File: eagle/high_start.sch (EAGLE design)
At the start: 37 parts, among them IC1 7805L, Q1 16Mhz, Q2 IRF510, Q3 IRF510, Q4 IRF510, U2 ATMEGA328P_PDIP

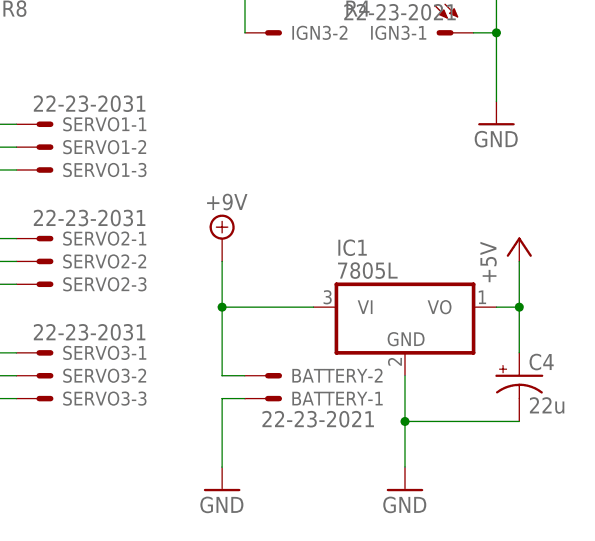
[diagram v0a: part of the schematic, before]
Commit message: pulldowns placed
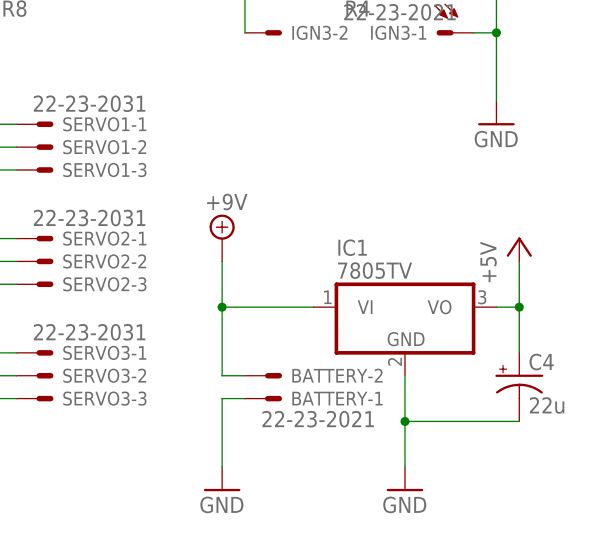
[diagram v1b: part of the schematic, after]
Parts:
- IC1: value 7805L -> 7805TV; device linear:7805L -> linear:7805TV
- R10, R6, R9: device rcl:R-US_0207/7 -> rcl:R-US_0207/2V
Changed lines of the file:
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@@
 <grid distance="0.1" unitdist="inch" unit="inch" style="lines" multiple="1" display="no" altdistance="0.01" altunitdist="inch" altunit="inch"/>
 <layers>
-<layer number="1" name="Top" color="4" fill="1" visible="no" active="no"/>
-<layer number="16" name="Bottom" color="1" fill="1" visible="no" active="no"/>
-<layer number="17" name="Pads" color="2" fill="1" visible="no" active="no"/>
-<layer number="18" name="Vias" color="2" fill="1" visible="no" active="no"/>
-<layer number="19" name="Unrouted" color="6" fill="1" visible="no" active="no"/>
-<layer number="20" name="Dimension" color="15" fill="1" visible="no" active="no"/>
-<layer number="21" name="tPlace" color="7" fill="1" visible="no" active="no"/>
-<layer number="22" name="bPlace" color="7" fill="1" visible="no" active="no"/>
-<layer number="23" name="tOrigins" color="15" fill="1" visible="no" active="no"/>
-<layer number="24" name="bOrigins" color="15" fill="1" visible="no" active="no"/>
-<layer number="25" name="tNames" color="7" fill="1" visible="no" active="no"/>
-<layer number="26" name="bNames" color="7" fill="1" visible="no" active="no"/>
-<layer number="27" name="tValues" color="7" fill="1" visible="no" active="no"/>
-<layer number="28" name="bValues" color="7" fill="1" visible="no" active="no"/>
+<layer number="1" name="Top" color="4" fill="1" visible="yes" active="no"/>
+<layer number="16" name="Bottom" color="1" fill="1" visible="yes" active="no"/>
+<layer number="17" name="Pads" color="2" fill="1" visible="yes" active="no"/>
+<layer number="18" name="Vias" color="2" fill="1" visible="yes" active="no"/>
+<layer number="19" name="Unrouted" color="6" fill="1" visible="yes" active="no"/>
+<layer number="20" name="Dimension" color="15" fill="1" visible="yes" active="no"/>
+<layer number="21" name="tPlace" color="7" fill="1" visible="yes" active="no"/>
+<layer number="22" name="bPlace" color="7" fill="1" visible="yes" active="no"/>
+<layer number="23" name="tOrigins" color="15" fill="1" visible="yes" active="no"/>
+<layer number="24" name="bOrigins" color="15" fill="1" visible="yes" active="no"/>
+<layer number="25" name="tNames" color="7" fill="1" visible="yes" active="no"/>
+<layer number="26" name="bNames" color="7" fill="1" visible="yes" active="no"/>
+<layer number="27" name="tValues" color="7" fill="1" visible="yes" active="no"/>
+<layer number="28" name="bValues" color="7" fill="1" visible="yes" active="no"/>
 <layer number="29" name="tStop" color="7" fill="3" visible="no" active="no"/>
 <layer number="30" name="bStop" color="7" fill="6" visible="no" active="no"/>
@@
 <layer number="35" name="tGlue" color="7" fill="4" visible="no" active="no"/>
 <layer number="36" name="bGlue" color="7" fill="5" visible="no" active="no"/>
-<layer number="37" name="tTest" color="7" fill="1" visible="no" active="no"/>
-<layer number="38" name="bTest" color="7" fill="1" visible="no" active="no"/>
+<layer number="37" name="tTest" color="7" fill="1" visible="yes" active="no"/>
+<layer number="38" name="bTest" color="7" fill="1" visible="yes" active="no"/>
 <layer number="39" name="tKeepout" color="4" fill="11" visible="no" active="no"/>
 <layer number="40" name="bKeepout" color="1" fill="11" visible="no" active="no"/>
@@
 <layer number="44" name="Drills" color="7" fill="1" visible="no" active="no"/>
 <layer number="45" name="Holes" color="7" fill="1" visible="no" active="no"/>
-<layer number="46" name="Milling" color="3" fill="1" visible="no" active="no"/>
-<layer number="47" name="Measures" color="7" fill="1" visible="no" active="no"/>
-<layer number="48" name="Document" color="7" fill="1" visible="no" active="no"/>
-<layer number="49" name="Reference" color="7" fill="1" visible="no" active="no"/>
-<layer number="50" name="dxf" color="7" fill="1" visible="no" active="no"/>
-<layer number="51" name="tDocu" color="7" fill="1" visible="no" active="no"/>
-<layer number="52" name="bDocu" color="7" fill="1" visible="no" active="no"/>
-<layer number="53" name="tGND_GNDA" color="7" fill="9" visible="no" active="no"/>
-<layer number="54" name="bGND_GNDA" color="1" fill="9" visible="no" active="no"/>
-<layer number="56" name="wert" color="7" fill="1" visible="no" active="no"/>
-<layer number="57" name="tCAD" color="7" fill="1" visible="no" active="no"/>
-<layer number="59" name="tCarbon" color="7" fill="1" visible="no" active="no"/>
-<layer number="60" name="bCarbon" color="7" fill="1" visible="no" active="no"/>
+<layer number="46" name="Milling" color="3" fill="1" visible="yes" active="no"/>
+<layer number="47" name="Measures" color="7" fill="1" visible="yes" active="no"/>
+<layer number="48" name="Document" color="7" fill="1" visible="yes" active="no"/>
+<layer number="49" name="Reference" color="7" fill="1" visible="yes" active="no"/>
+<layer number="50" name="dxf" color="7" fill="1" visible="yes" active="no"/>
+<layer number="51" name="tDocu" color="7" fill="1" visible="yes" active="no"/>
+<layer number="52" name="bDocu" color="7" fill="1" visible="yes" active="no"/>
+<layer number="53" name="tGND_GNDA" color="7" fill="9" visible="yes" active="no"/>
+<layer number="54" name="bGND_GNDA" color="1" fill="9" visible="yes" active="no"/>
+<layer number="56" name="wert" color="7" fill="1" visible="yes" active="no"/>
+<layer number="57" name="tCAD" color="7" fill="1" visible="yes" active="no"/>
+<layer number="59" name="tCarbon" color="7" fill="1" visible="yes" active="no"/>
+<layer number="60" name="bCarbon" color="7" fill="1" visible="yes" active="no"/>
 <layer number="90" name="Modules" color="5" fill="1" visible="yes" active="yes"/>
 <layer number="91" name="Nets" color="2" fill="1" visible="yes" active="yes"/>
@@
 <part name="P+5" library="supply1" deviceset="+5V" device=""/>
 <part name="GND7" library="supply1" deviceset="GND" device=""/>
-<part name="IC1" library="linear" deviceset="78*" device="L" technology="05"/>
+<part name="IC1" library="linear" deviceset="78*" device="TV" technology="05" value="7805TV"/>
 <part name="SUPPLY2" library="supply2" deviceset="+9V" device=""/>
 <part name="C4" library="rcl" deviceset="CPOL-US" device="B45181A" value="22u"/>
@@
 <part name="GND9" library="supply1" deviceset="GND" device=""/>
 <part name="R5" library="rcl" deviceset="R-US_" device="0207/7" value="220"/>
-<part name="R6" library="rcl" deviceset="R-US_" device="0207/7" value="10k"/>
+<part name="R6" library="rcl" deviceset="R-US_" device="0207/2V" value="10k"/>
 <part name="R7" library="rcl" deviceset="R-US_" device="0207/7" value="220"/>
 <part name="R8" library="rcl" deviceset="R-US_" device="0207/7" value="220"/>
-<part name="R9" library="rcl" deviceset="R-US_" device="0207/7" value="10k"/>
-<part name="R10" library="rcl" deviceset="R-US_" device="0207/7" value="10k"/>
+<part name="R9" library="rcl" deviceset="R-US_" device="0207/2V" value="10k"/>
+<part name="R10" library="rcl" deviceset="R-US_" device="0207/2V" value="10k"/>
 <part name="GND5" library="supply1" deviceset="GND" device=""/>
 </parts>

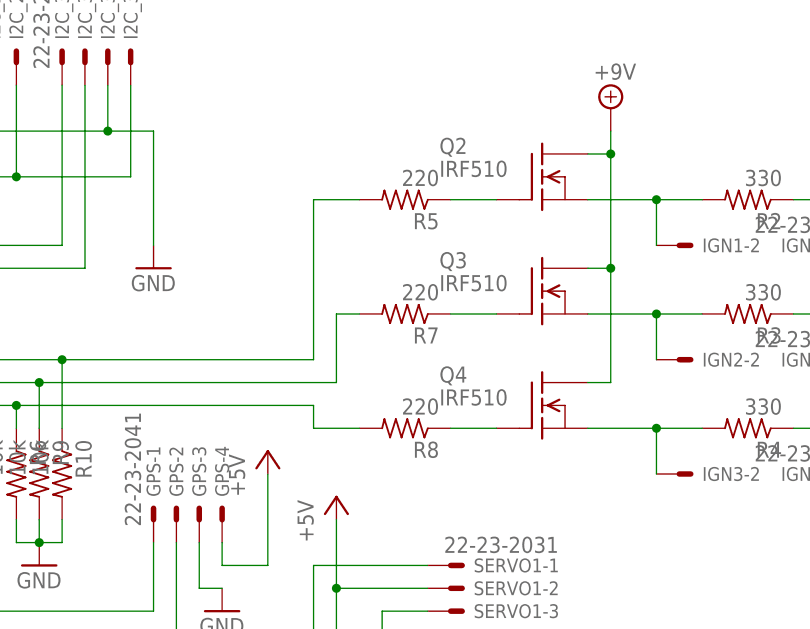
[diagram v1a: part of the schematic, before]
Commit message: moved fets up to Vbatt for igniter5 worky
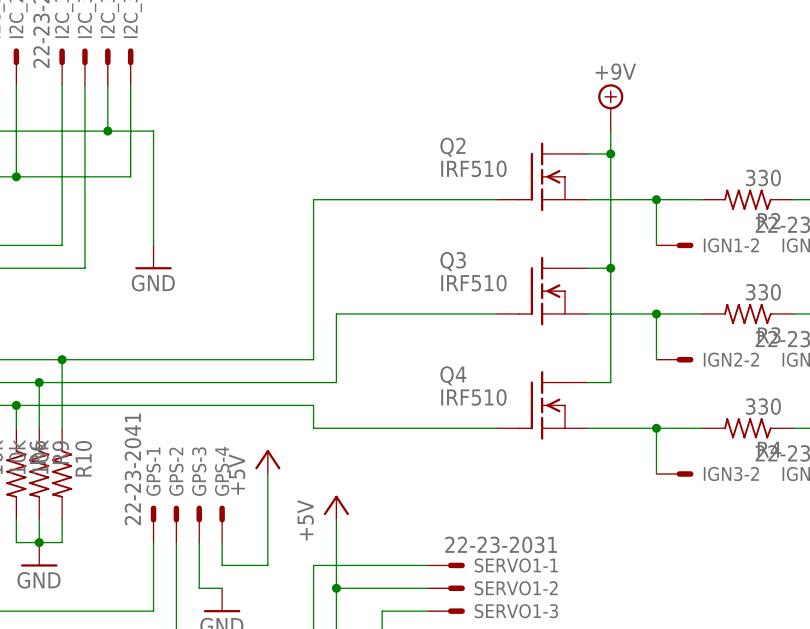
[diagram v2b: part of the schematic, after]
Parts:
- removed R5, R7, R8: 220, rcl:R-US_0207/7
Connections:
- removed net N$12: Q2.G, R5.1
- removed net N$13: Q3.G, R7.1
- removed net N$14: Q4.G, R8.1
- net N$18: now also Q2.G; no longer R5.2
- net N$19: now also Q3.G; no longer R7.2
- net N$20: now also Q4.G; no longer R8.2
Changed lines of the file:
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@@
 <?xml version="1.0" encoding="utf-8"?>
 <!DOCTYPE eagle SYSTEM "eagle.dtd">
-<eagle version="7.7.0">
+<eagle version="7.6.0">
 <drawing>
 <settings>
@@
 <part name="BATTERY" library="con-molex" deviceset="22-23-2021" device=""/>
 <part name="GND9" library="supply1" deviceset="GND" device=""/>
-<part name="R5" library="rcl" deviceset="R-US_" device="0207/7" value="220"/>
 <part name="R6" library="rcl" deviceset="R-US_" device="0207/2V" value="10k"/>
-<part name="R7" library="rcl" deviceset="R-US_" device="0207/7" value="220"/>
-<part name="R8" library="rcl" deviceset="R-US_" device="0207/7" value="220"/>
 <part name="R9" library="rcl" deviceset="R-US_" device="0207/2V" value="10k"/>
 <part name="R10" library="rcl" deviceset="R-US_" device="0207/2V" value="10k"/>
@@
 <instance part="BATTERY" gate="-2" x="124.46" y="22.86" rot="MR180"/>
 <instance part="GND9" gate="1" x="119.38" y="10.16"/>
-<instance part="R5" gate="G$1" x="93.98" y="91.44" rot="R180"/>
 <instance part="R6" gate="G$1" x="50.8" y="60.96" rot="R270"/>
-<instance part="R7" gate="G$1" x="93.98" y="78.74" rot="R180"/>
-<instance part="R8" gate="G$1" x="93.98" y="66.04" rot="R180"/>
 <instance part="R9" gate="G$1" x="53.34" y="60.96" rot="R270"/>
 <instance part="R10" gate="G$1" x="55.88" y="60.96" rot="R270"/>
@@
 <wire x1="55.88" y1="73.66" x2="83.82" y2="73.66" width="0.1524" layer="91"/>
 <wire x1="83.82" y1="73.66" x2="83.82" y2="91.44" width="0.1524" layer="91"/>
-<wire x1="83.82" y1="91.44" x2="88.9" y2="91.44" width="0.1524" layer="91"/>
-<pinref part="R5" gate="G$1" pin="2"/>
 <pinref part="R10" gate="G$1" pin="1"/>
 <wire x1="55.88" y1="66.04" x2="55.88" y2="73.66" width="0.1524" layer="91"/>
 <junction x="55.88" y="73.66"/>
+<pinref part="Q2" gate="G$1" pin="G"/>
+<wire x1="83.82" y1="91.44" x2="104.14" y2="91.44" width="0.1524" layer="91"/>
 </segment>
 </net>
@@
 <wire x1="53.34" y1="71.12" x2="86.36" y2="71.12" width="0.1524" layer="91"/>
 <wire x1="86.36" y1="71.12" x2="86.36" y2="78.74" width="0.1524" layer="91"/>
-<wire x1="86.36" y1="78.74" x2="88.9" y2="78.74" width="0.1524" layer="91"/>
-<pinref part="R7" gate="G$1" pin="2"/>
+<wire x1="86.36" y1="78.74" x2="104.14" y2="78.74" width="0.1524" layer="91"/>
 <pinref part="R9" gate="G$1" pin="1"/>
 <wire x1="53.34" y1="66.04" x2="53.34" y2="71.12" width="0.1524" layer="91"/>
 <junction x="53.34" y="71.12"/>
+<pinref part="Q3" gate="G$1" pin="G"/>
 </segment>
 </net>
@@
 <wire x1="50.8" y1="68.58" x2="83.82" y2="68.58" width="0.1524" layer="91"/>
 <wire x1="83.82" y1="68.58" x2="83.82" y2="66.04" width="0.1524" layer="91"/>
-<wire x1="83.82" y1="66.04" x2="88.9" y2="66.04" width="0.1524" layer="91"/>
-<pinref part="R8" gate="G$1" pin="2"/>
 <pinref part="R6" gate="G$1" pin="1"/>
 <wire x1="50.8" y1="66.04" x2="50.8" y2="68.58" width="0.1524" layer="91"/>
 <junction x="50.8" y="68.58"/>
+<pinref part="Q4" gate="G$1" pin="G"/>
+<wire x1="83.82" y1="66.04" x2="104.14" y2="66.04" width="0.1524" layer="91"/>
 </segment>
 </net>
@@
 </segment>
 </net>
-<net name="N$12" class="0">
-<segment>
-<pinref part="Q2" gate="G$1" pin="G"/>
-<pinref part="R5" gate="G$1" pin="1"/>
-<wire x1="99.06" y1="91.44" x2="104.14" y2="91.44" width="0.1524" layer="91"/>
-</segment>
-</net>
-<net name="N$13" class="0">
-<segment>
-<pinref part="Q3" gate="G$1" pin="G"/>
-<pinref part="R7" gate="G$1" pin="1"/>
-<wire x1="99.06" y1="78.74" x2="104.14" y2="78.74" width="0.1524" layer="91"/>
-</segment>
-</net>
-<net name="N$14" class="0">
-<segment>
-<pinref part="Q4" gate="G$1" pin="G"/>
-<pinref part="R8" gate="G$1" pin="1"/>
-<wire x1="99.06" y1="66.04" x2="104.14" y2="66.04" width="0.1524" layer="91"/>
-</segment>
-</net>
